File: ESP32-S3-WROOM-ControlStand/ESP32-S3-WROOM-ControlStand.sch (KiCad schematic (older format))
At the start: 43 parts, among them J1 Button & LED Panel, J2 Button & LED Panel, J3 STEMMA (Display), J4 Horn, J5 Brake, J6 Light Switch, J7 Reverser, J8 Throttle, P1 CONN_8, P2 Misc buttons, bell, status LED, P3 CONN_3, P4 CONN_3, P5 CONN_5, P6 CONN_3, P7 CONN_3, SW1 A, SW2 B, SW3 C, SW4 D, SW5 Bell, SW6 LIGHT_SWITCH

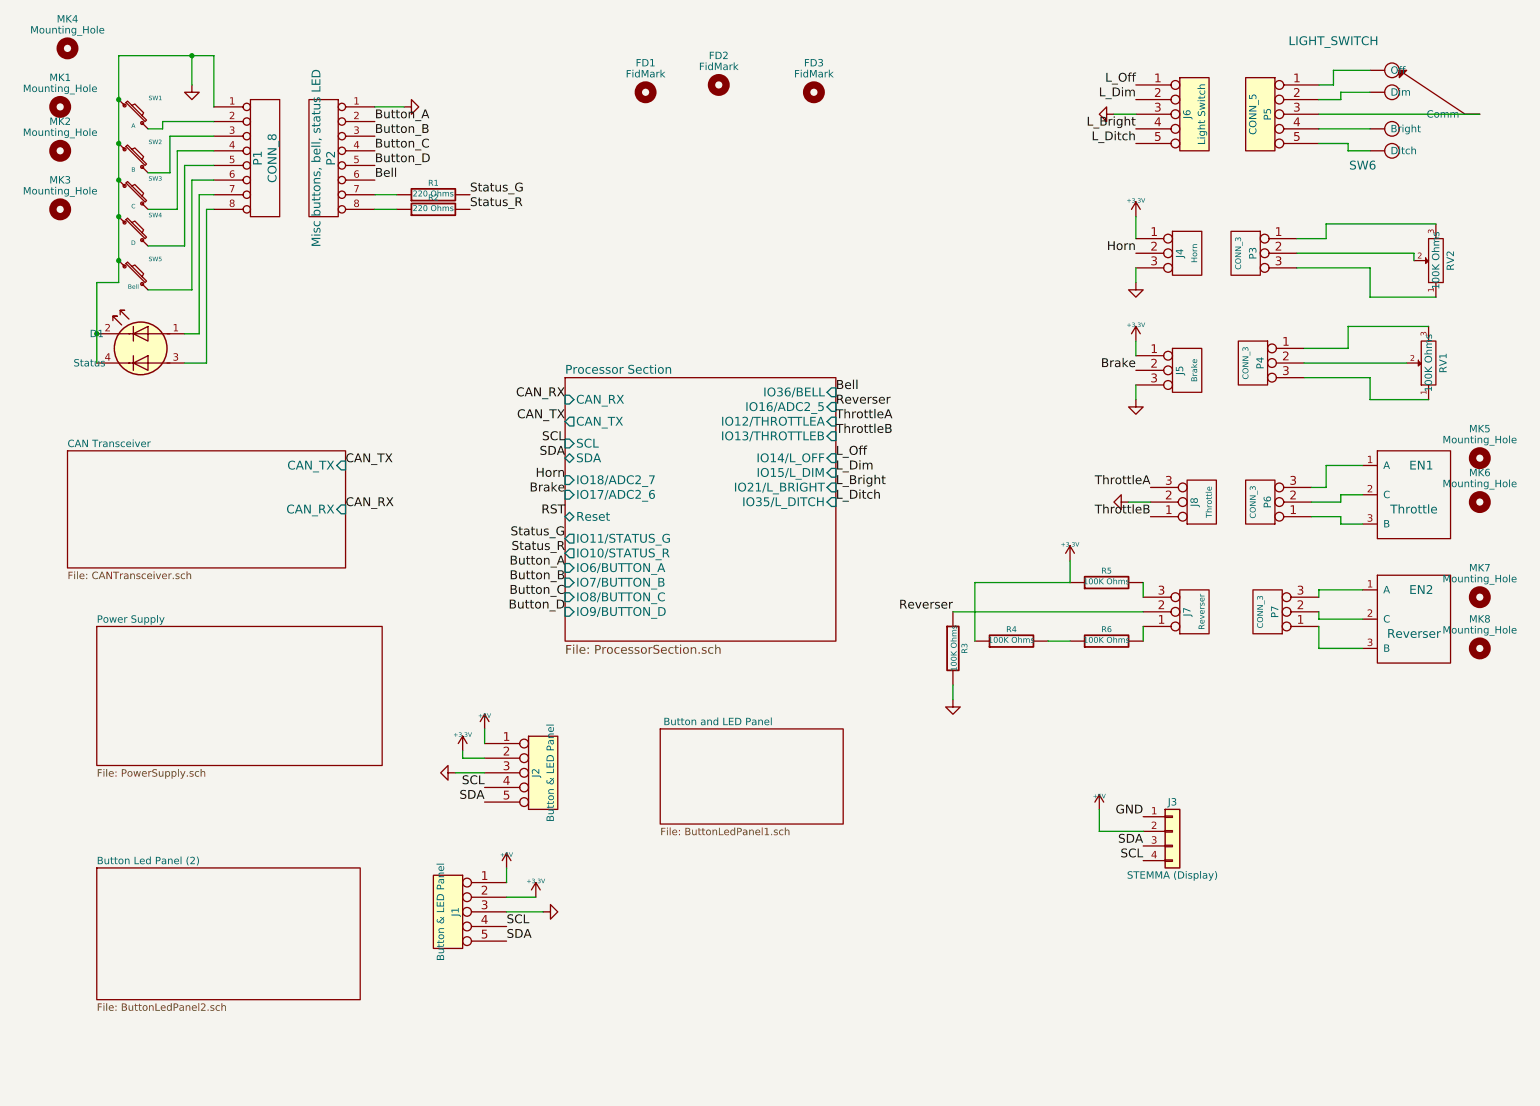
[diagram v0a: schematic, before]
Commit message: Add Keypad board.
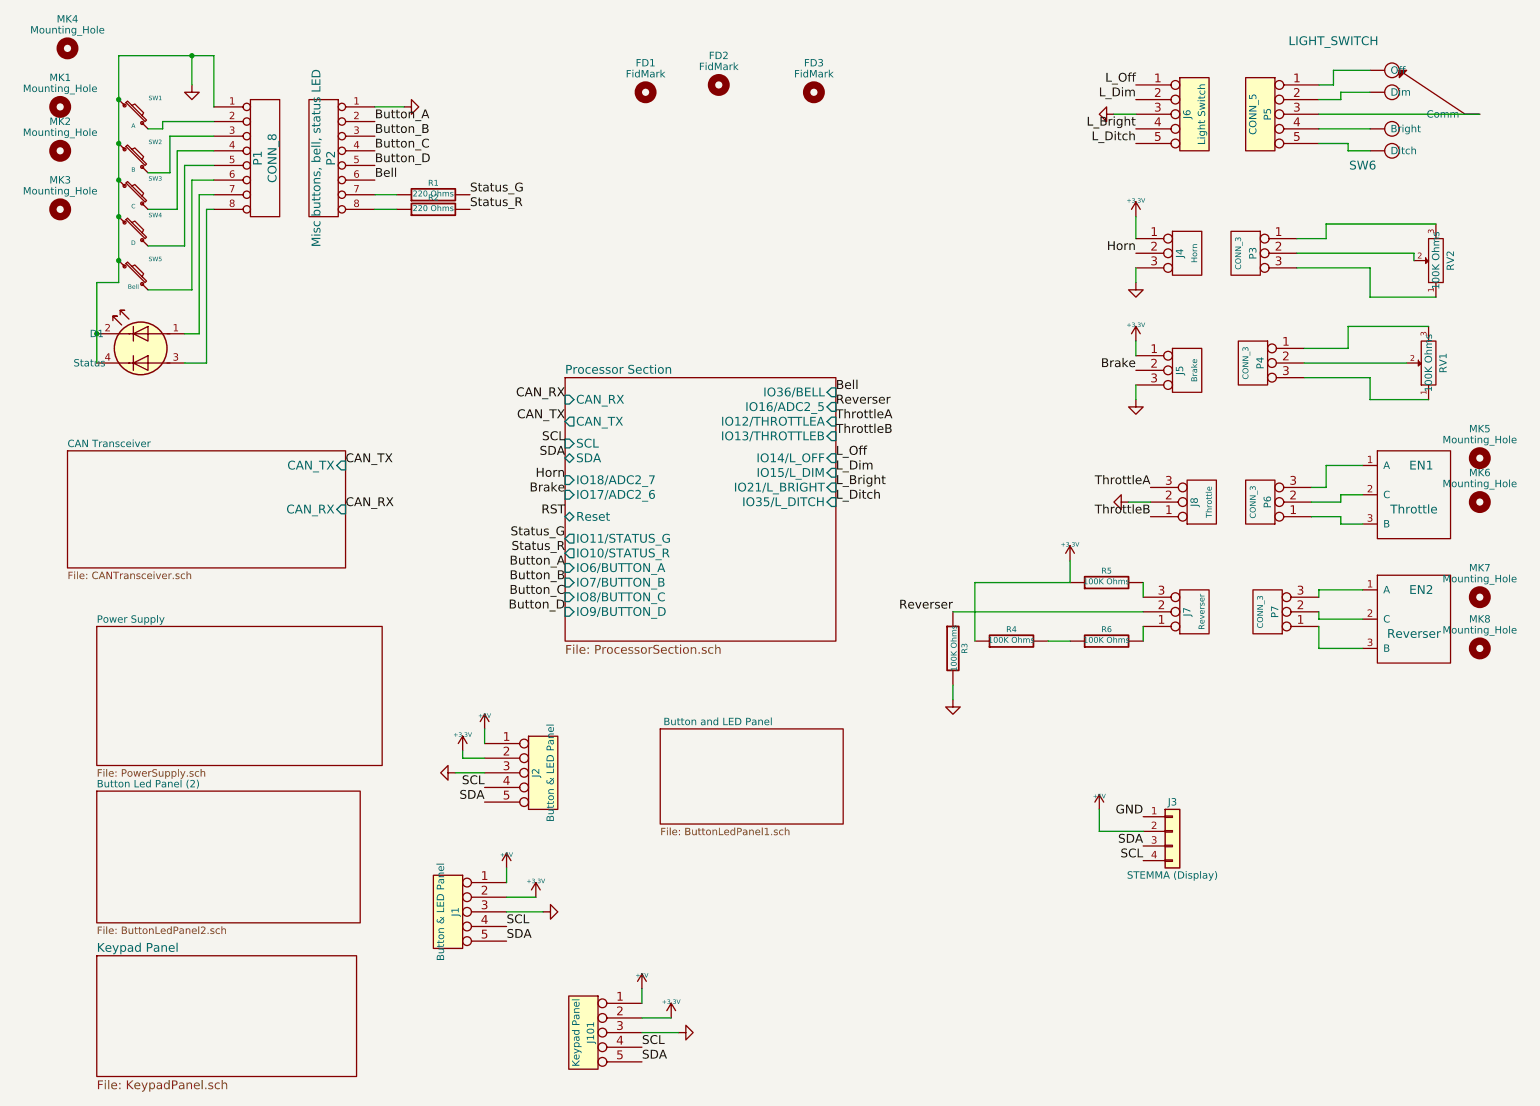
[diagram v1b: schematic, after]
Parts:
- added J101: Keypad Panel, Pin_Headers:Pin_Header_Straight_1x05_Pitch2.54mm, symbol CONN_5
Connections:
- net +3V3: now also J101.2
- net +5V: now also J101.1
- net GND: now also J101.3
- net SCL: now also J101.4
- net SDA: now also J101.5
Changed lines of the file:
@@
 LIBS:gct_usb4105
 LIBS:USBLC6-2SC6
+LIBS:tca8418
+LIBS:sw_push_small_gnd
 LIBS:ESP32-S3-WROOM-ControlStand-cache
 EELAYER 25 0
@@
 $Descr USLetter 11000 8500
 encoding utf-8
-Sheet 1 6
+Sheet 1 7
 Title "ESP32-S3-WROOM-ControlStand"
 Date "2022-07-25"
@@
 $EndComp
 $Sheet
-S 900  6450 1800 900
+S 900  5925 1800 900
 U 62DF043D
 F0 "Button Led Panel (2)" 50
@@
 Connection ~ 1050 2300
 Wire Wire Line
-	1700 1250 1700 900
-Wire Wire Line
-	1700 900  1050 900
+	1700 900  1700 1250
+Wire Wire Line
+	1050 900  1700 900
 Connection ~ 1050 1200
 Wire Wire Line
@@
 Wire Wire Line
 	9550 4550 9250 4550
+$Comp
+L CONN_5 J101
+U 1 1 6394B610
+P 4225 7575
+F 0 "J101" V 4175 7575 50  0000 C CNN
+F 1 "Keypad Panel" V 4275 7575 50  0000 C CNN
+F 2 "Pin_Headers:Pin_Header_Straight_1x05_Pitch2.54mm" H 4225 7575 60  0001 C CNN
+F 3 "~" H 4225 7575 60  0000 C CNN
+F 4 "523-G800W303018EU" V 4225 7575 60  0001 C CNN "Mouser Part Number"
+	1    4225 7575
+	-1   0    0    -1
+$EndComp
+Text Label 4625 7675 0    60   ~ 0
+SCL
+Text Label 4625 7775 0    60   ~ 0
+SDA
+$Comp
+L +5V #PWR018
+U 1 1 6394B618
+P 4625 7275
+F 0 "#PWR018" H 4625 7365 20  0001 C CNN
+F 1 "+5V" H 4625 7365 30  0000 C CNN
+F 2 "" H 4625 7275 60  0000 C CNN
+F 3 "" H 4625 7275 60  0000 C CNN
+	1    4625 7275
+	-1   0    0    -1
+$EndComp
+$Comp
+L +3.3V #PWR019
+U 1 1 6394B61E
+P 4825 7475
+F 0 "#PWR019" H 4825 7435 30  0001 C CNN
+F 1 "+3.3V" H 4825 7585 30  0000 C CNN
+F 2 "" H 4825 7475 60  0000 C CNN
+F 3 "" H 4825 7475 60  0000 C CNN
+	1    4825 7475
+	1    0    0    -1
+$EndComp
+$Comp
+L GND #PWR020
+U 1 1 6394B624
+P 4875 7575
+F 0 "#PWR020" H 4875 7575 30  0001 C CNN
+F 1 "GND" H 4875 7505 30  0001 C CNN
+F 2 "" H 4875 7575 60  0000 C CNN
+F 3 "" H 4875 7575 60  0000 C CNN
+	1    4875 7575
+	0    -1   -1   0
+$EndComp
+Wire Wire Line
+	4625 7275 4625 7375
+Wire Wire Line
+	4625 7475 4825 7475
+Wire Wire Line
+	4625 7575 4875 7575
+$Sheet
+S 900  7050 1775 825
+U 6394C805
+F0 "Keypad Panel" 60
+F1 "KeypadPanel.sch" 60
+$EndSheet
 $EndSCHEMATC
